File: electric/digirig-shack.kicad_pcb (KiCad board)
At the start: 2 copper layers, 80 x 50 mm, 63 parts, among them J1 USB_B_Micro, J2 USB_A, J3 PTT/CW, J4 Serial, J5 Audio, T1 600/600 Audio, T2 600/600 Audio, U1 TUSB2046, U2 CM108, U3 CP2102N-A01, U4 PC817, U5 PC817, Y1 6MHz, Y2 12MHz

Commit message: Rev 1.1 Mods Continued
Compressed mobile version to 23mm width
Added pulldown resistors on secondary USB ports in shack version
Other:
- board text added: "Rev 1.1"
- board text added: "by KW0X"
- board text added: "digirig shack"
- board text removed: "Rev 1.0"
- board text removed: "by KF0BAY"
- board text removed: "digirig"

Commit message: Revision 1.3 updates
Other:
- board text added: "by K0TX"
- board text removed: "by KW0X"

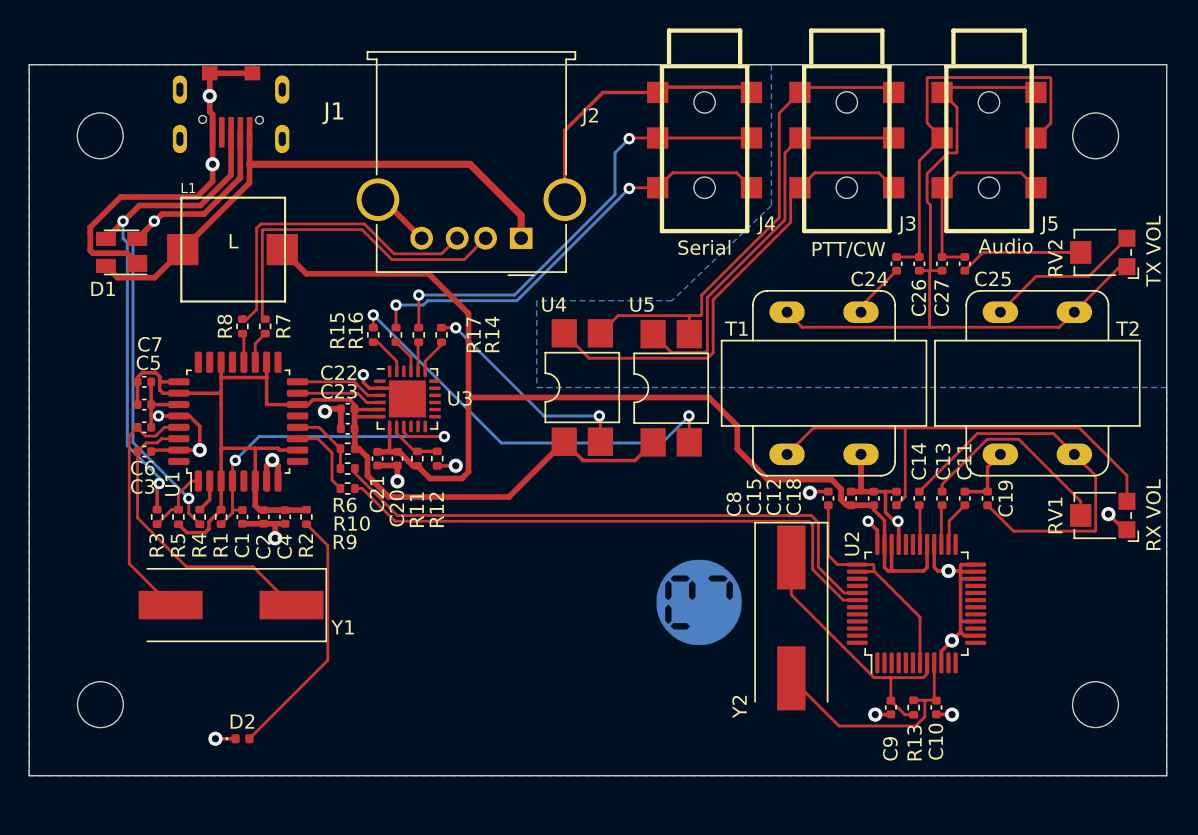
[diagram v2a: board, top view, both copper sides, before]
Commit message: Digirig Shack Rev 1.1
- 51mm wide board for sized aluminum case
- electric insulation on PC side instead of audio transformers
- Full size USB B connector on PC side
- RJ45 connector on rig side
- DIP socket for connector pinout configuration
- additional audio and serial pins as headers
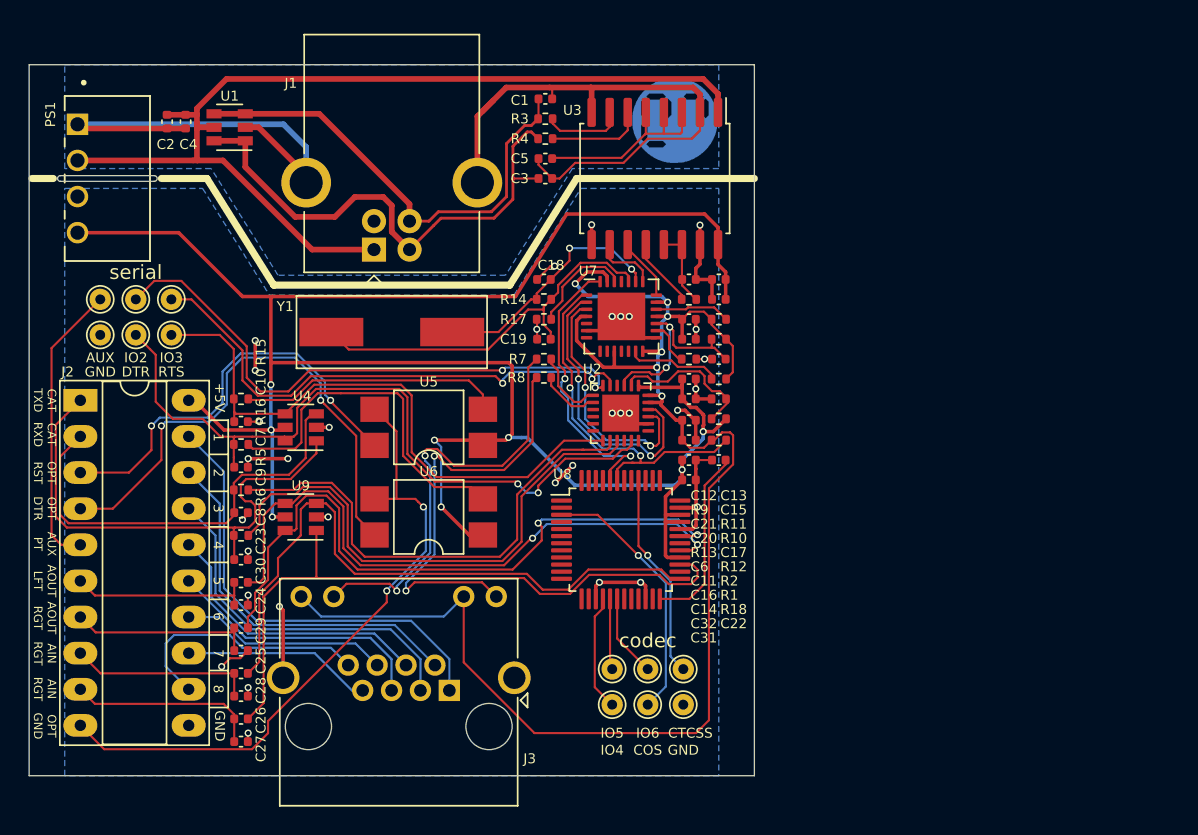
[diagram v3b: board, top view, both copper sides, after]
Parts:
- removed the C11 at (205.8, 69.5)
- removed the C14 at (202.6, 69.5)
- removed the C6 at (148.1, 64.5)
- removed D1: SP0503BAHT, Package_TO_SOT_SMD:SOT-143
- removed D2: PWR (RED), LED_SMD:LED_0402_1005Metric
- removed J4: Serial, footprints:jack_3.5_pj313d-smt
- removed J5: Audio, footprints:jack_3.5_pj313d-smt
- removed the R10 at (162.4, 67.4)
- removed RV1, RV2: 10K, Potentiometer_SMD:Potentiometer_Bourns_TC33X_Vertical
- removed Ref**: Val**, footprints:QR-code
- removed Ref**: Val**, footprints:digirig-logo-6mm
- removed T1, T2: 600/600 Audio, footprints:Audio_Transformer
- removed the U2 at (202.4, 76.9)
- removed Y2: 12MHz, Crystal:Crystal_SMD_HC49-SD
- added C1: 47pF, Capacitor_SMD:C_0402_1005Metric, F.Cu at (176.3, 41.4)
- added C2: 10uF, Capacitor_SMD:C_0402_1005Metric, F.Cu at (149.7, 43.0)
- added C22: 10uF, Capacitor_SMD:C_0402_1005Metric, F.Cu at (188.5, 66.8)
- added C23: 10uF, Capacitor_SMD:C_0402_1005Metric, F.Cu at (154.9, 75.4)
- added C28: 47pF, Capacitor_SMD:C_0402_1005Metric, F.Cu at (154.9, 83.4)
- added C29: 47pF, Capacitor_SMD:C_0402_1005Metric, F.Cu at (154.9, 80.2)
- added C30: 47pF, Capacitor_SMD:C_0402_1005Metric, F.Cu at (154.9, 77.0)
- added C31: 10uF, Capacitor_SMD:C_0402_1005Metric, F.Cu at (186.4, 68.2)
- added C32: 100nF, Capacitor_SMD:C_0402_1005Metric, F.Cu at (186.4, 66.8)
- added C4: 100nF, Capacitor_SMD:C_0402_1005Metric, F.Cu at (151.0, 43.0)
- added PS1: B0505S-1WR2, footprints:CONV_B0505S-1WR2, F.Cu at (145.5, 47.0)
- added R1: 22K, Resistor_SMD:R_0402_1005Metric, F.Cu at (188.5, 63.9)
- added R18: 1.5K, Resistor_SMD:R_0402_1005Metric, F.Cu at (188.5, 65.4)
- added TP1: IO3, TestPoint:TestPoint_THTPad_D1.5mm_Drill0.7mm, F.Cu at (150.0, 55.5)
- added TP10: IO6, TestPoint:TestPoint_THTPad_D1.5mm_Drill0.7mm, F.Cu at (183.5, 81.5)
- added TP11: GND, TestPoint:TestPoint_THTPad_D1.5mm_Drill0.7mm, F.Cu at (186.0, 84.0)
- added TP12: GND, TestPoint:TestPoint_THTPad_D1.5mm_Drill0.7mm, F.Cu at (145.0, 58.0)
- added TP2: IO2, TestPoint:TestPoint_THTPad_D1.5mm_Drill0.7mm, F.Cu at (147.5, 55.5)
- added TP3: RTS, TestPoint:TestPoint_THTPad_D1.5mm_Drill0.7mm, F.Cu at (150.0, 58.0)
- added TP4: DTR, TestPoint:TestPoint_THTPad_D1.5mm_Drill0.7mm, F.Cu at (147.5, 58.0)
- added TP5: AUX, TestPoint:TestPoint_THTPad_D1.5mm_Drill0.7mm, F.Cu at (145.0, 55.5)
- added TP6: COS, TestPoint:TestPoint_THTPad_D1.5mm_Drill0.7mm, F.Cu at (183.5, 84.0)
- added TP7: CTCSS, TestPoint:TestPoint_THTPad_D1.5mm_Drill0.7mm, F.Cu at (186.0, 81.5)
- added TP8: IO4, TestPoint:TestPoint_THTPad_D1.5mm_Drill0.7mm, F.Cu at (181.0, 84.0)
- added TP9: IO5, TestPoint:TestPoint_THTPad_D1.5mm_Drill0.7mm, F.Cu at (181.0, 81.5)
- added U3: ADUM3160, Package_SO:SOIC-16W_7.5x10.3mm_P1.27mm, F.Cu at (184.0, 47.0)
- added U4: ESDU5V0H4, Package_TO_SOT_SMD:SOT-23-6, F.Cu at (159.1, 64.5)
- added U7: USB2412-DZK-TR, Package_DFN_QFN:QFN-28-1EP_5x5mm_P0.5mm_EP3.35x3.35mm, F.Cu at (181.7, 56.7)
- added U8: CM118B, Package_QFP:LQFP-48_7x7mm_P0.5mm, F.Cu at (181.6, 72.4)
- added U9: ESDU5V0H4, Package_TO_SOT_SMD:SOT-23-6, F.Cu at (159.1, 70.8)
- C10, C3, C9: value 27pF -> 47pF
- C12: value 10uF -> 100nF
- C18, C19: value 100pF -> 27pF
- C26: value 100pF -> 10uF
- C27: value 100pF -> 47pF
- C7: value 100nF -> 47pF
- C8: value 10uF -> 47pF
- J1: value USB_B_Micro -> USB_B; footprint footprints:USB_MICRO_A01SB141B1-298 -> Connector_USB:USB_B_OST_USB-B1HSxx_Horizontal
- J2: value USB_A -> Socket_20DIP; footprint Connector_USB:USB_A_Molex_67643_Horizontal -> Package_DIP:DIP-20_W7.62mm_Socket_LongPads
- J3: value PTT/CW -> RJ45_LED_Shielded; footprint footprints:jack_3.5_pj313d-smt -> Connector_RJ:RJ45_Amphenol_RJHSE538X
- L1: value 2.2mH -> LOGO; footprint footprints:CD74R -> footprints:digirig-logo-6mm
- R11: value 22K -> 100K
- R12: value 47K -> 100K
- R13: value 1M -> 100K
- R14: value 470 -> 1M
- R16, R7, R8: value 33 -> 470
- R17: value 33 -> 12K
- R2: value 1K -> 47K
- R5, R6: value 1.5K -> 33
- R9: value 33 -> 10K
- U1: value TUSB2046 -> ESDU5V0H4; footprint Package_QFP:LQFP-32_7x7mm_P0.8mm -> Package_TO_SOT_SMD:SOT-23-6
- Y1: value 6MHz -> 24MHz
- moved C27 59.7 mm to (154.9, 86.6), turned to 180 degrees
- moved C25 58.5 mm to (154.9, 81.8), turned to 0 degrees
- moved C26 57.4 mm to (154.9, 85.0), turned to 0 degrees
- moved C10 52.9 mm to (154.9, 64.1), turned to 180 degrees
- moved C24 52.7 mm to (154.9, 78.6), turned to 0 degrees
- moved C9 47.7 mm to (154.9, 70.5), turned to 180 degrees
- moved J3 47.3 mm to (169.6, 83.0)
- moved C8 41.5 mm to (154.9, 73.8), turned to 180 degrees
- moved R3 39.1 mm to (176.3, 42.8), turned to 180 degrees
- moved R10 37.2 mm to (188.5, 58.3), turned to 0 degrees
- moved R4 36.0 mm to (176.3, 44.2), turned to 180 degrees
- moved C17 35.3 mm to (188.5, 59.7), turned to 180 degrees
- moved C3 34.1 mm to (176.3, 47.0)
- moved C19 33.1 mm to (176.2, 58.3), turned to 180 degrees
- moved C5 33.1 mm to (176.3, 45.6), turned to 180 degrees
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- renumbered C21 to C11, C22 to C14, C23 to C16, C1 to C17, C2 to C20, C4 to C21, C20 to C6, R1 to R10, U3 to U2, U4 to U5, U5 to U6
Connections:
- C10 pad 1: Net-(C10-Pad1) -> GND
- C10 pad 2: GND -> ~RTS
- C12 pad 1: +5V -> Net-(C12-Pad1)
- C13 pad 1: Net-(C13-Pad1) -> +5V
- C13 pad 2: Net-(C13-Pad2) -> GND
- C17 pad 1: /~RESET -> ~RESET
- C19 pad 1: GND -> Net-(C19-Pad1)
- C19 pad 2: Net-(C14-Pad1) -> GND
- C24 pad 1: /AIN -> AFOUT_RIGHT
- C25 pad 1: /AOUT -> AFIN_LEFT
- C26 pad 1: /AIN -> AFIN_RIGHT
- C26 pad 2: /IGND -> Net-(C26-Pad2)
- C27 pad 1: /IGND -> GND
- C27 pad 2: /AOUT -> AFIN_RIGHT
- C3 pad 1: Net-(C3-Pad1) -> /PC_N
- C3 pad 2: GND -> GND1
- C5 pad 1: +3V3 -> Net-(C5-Pad1)
- C5 pad 2: GND -> GND1
- C7 pad 1: +3V3 -> GND
- C7 pad 2: GND -> ~DTR
- C8 pad 1: Net-(C8-Pad1) -> GND
- C8 pad 2: GND -> TxD
- C9 pad 1: Net-(C9-Pad1) -> GND
- C9 pad 2: GND -> RxD
- J1 pad 1: /RAW5V -> +5P
- J1 pad 2: /DM_RAW -> /PC_N
- J1 pad 3: /DP_RAW -> /PC_P
- J1 pad 4: Net-(J1-Pad4) -> GND1
- J1 pad 5: GND -> GND1
- J2 pad 1: /RAW5V -> TxD
- J2 pad 2: Net-(J2-Pad2) -> RxD
- J2 pad 3: Net-(J2-Pad3) -> ~PTT
- J2 pad 4: GND -> ~KEY
- J2 pad 5: GND -> Net-(J2-Pad5)
- R10 pad 1: /~RESET -> ~RESET
- R11 pad 1: +5V -> +3V3
- R12 pad 1: Net-(R11-Pad2) -> +3V3
- R12 pad 2: GND -> Net-(R12-Pad2)
- R13 pad 1: Net-(C10-Pad1) -> Net-(R13-Pad1)
- R13 pad 2: Net-(C9-Pad1) -> GND
- R14 pad 1: Net-(R14-Pad1) -> Net-(C19-Pad1)
- R14 pad 2: Net-(R14-Pad2) -> Net-(C18-Pad1)
- R15 pad 2: Net-(R15-Pad2) -> ~RTS
- R16 pad 1: Net-(J4-PadT) -> Net-(R16-Pad1)
- R16 pad 2: Net-(R16-Pad2) -> ~DTR
- R17 pad 2: Net-(R17-Pad2) -> GND
- R2 pad 1: Net-(D2-Pad2) -> Net-(R1-Pad2)
- R2 pad 2: +3V3 -> GND
- R3 pad 2: /DP_RAW -> /PC_P
- R4 pad 2: /DM_RAW -> /PC_N
- R5 pad 1: Net-(R3-Pad1) -> RxD
- R5 pad 2: +3V3 -> Net-(R5-Pad2)
- R6 pad 1: Net-(R10-Pad2) -> TxD
- R6 pad 2: +3V3 -> Net-(R6-Pad2)
- R7 pad 1: Net-(J2-Pad2) -> ~RX_LED
- R8 pad 1: Net-(J2-Pad3) -> ~TX_LED
- R9 pad 1: Net-(R9-Pad1) -> Net-(C12-Pad1)
- U1 pad 1: Net-(R3-Pad1) -> /PC_N
- U1 pad 2: Net-(R4-Pad1) -> GND1
- U1 pad 3: +3V3 -> /PC_P
- U1 pad 4: /~RESET -> /PC_P
- U1 pad 5: Net-(U1-Pad5) -> +5P
- U1 pad 6: +3V3 -> /PC_N
- U2 pad 1: Net-(U3-Pad1) -> (no net)
- U2 pad 10: Net-(U3-Pad10) -> (no net)
- U2 pad 13: /~RX_LED -> Net-(R7-Pad2)
- U2 pad 14: /~TX_LED -> Net-(R8-Pad2)
- U2 pad 15: Net-(U3-Pad15) -> (no net)
- U2 pad 16: Net-(U3-Pad16) -> (no net)
- U2 pad 17: Net-(U3-Pad17) -> (no net)
- U2 pad 18: Net-(U3-Pad18) -> (no net)
- U2 pad 19: Net-(R14-Pad2) -> ~RTS
- U2 pad 20: Net-(R17-Pad2) -> Net-(R5-Pad2)
- U2 pad 21: Net-(R16-Pad2) -> Net-(R6-Pad2)
- U2 pad 22: Net-(U3-Pad22) -> (no net)
- U2 pad 23: Net-(R15-Pad2) -> ~DTR
- U2 pad 24: Net-(U3-Pad24) -> (no net)
- U2 pad 3: Net-(U1-Pad16) -> SRL_P
- U2 pad 4: Net-(U1-Pad15) -> SRL_N
- U2 pad 8: Net-(R11-Pad2) -> Net-(R1-Pad2)
- U2 pad 9: /~RESET -> ~RESET
- U5 pad 1: +3V3 -> +5V
- U5 pad 2: Net-(R14-Pad1) -> Net-(R15-Pad1)
- U5 pad 3: Net-(J3-PadS) -> GND2
- U5 pad 4: Net-(J3-PadT) -> ~PTT
- U6 pad 1: +3V3 -> +5V
- U6 pad 2: Net-(R15-Pad1) -> Net-(R16-Pad1)
- U6 pad 3: Net-(J3-PadS) -> GND2
- U6 pad 4: Net-(J3-PadR) -> ~KEY
- Y1 pad 1: Net-(C3-Pad1) -> Net-(C18-Pad1)
- Y1 pad 2: Net-(C6-Pad1) -> Net-(C19-Pad1)
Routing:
- net +5V: track 79.6 -> 154.3 mm, vias 0 -> 8
- net GND1: track 0.00 -> 74.4 mm
- net +5P: track 0.00 -> 69.6 mm
- net GND: track 122.1 -> 61.5 mm, vias 19 -> 33
- net /IGND: track 52.9 -> 0.00 mm
- net ~DTR: track 0.00 -> 52.1 mm, vias 0 -> 2
- net Net-(C26-Pad2): track 0.00 -> 46.9 mm
- net GND2: track 0.00 -> 45.5 mm, vias 0 -> 2
- net Net-(C23-Pad2): track 0.00 -> 43.9 mm, vias 0 -> 2
- net Net-(C24-Pad2): track 3.96 -> 47.1 mm, vias 0 -> 2
- net ~RTS: track 0.00 -> 42.9 mm
- net Net-(R10-Pad1): track 41.5 -> 0.00 mm
- net Net-(R9-Pad1): track 40.4 -> 0.00 mm
- net Net-(TP2-Pad1): track 0.00 -> 40.1 mm, vias 0 -> 2
- net /RAW5V: track 39.1 -> 0.00 mm
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- added copper zone on B.Cu, net GND1
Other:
- board size 80 x 50 mm -> 51 x 50 mm
- net class Default: clearance 0.2 -> 0.15; trace_width 0.2 -> 0.15; via_dia 0.8 -> 0.5; via_drill 0.4 -> 0.3
- net class Power: clearance 0.2 -> 0.15
- rule trace_clearance: 0.2 -> 0.15
- board text added: "+5V"
- board text added: "1"
- board text added: "2"
- board text added: "3"
- board text added: "4"
- board text added: "5"
- board text added: "6"
- board text added: "7"
- board text added: "8"
- board text added: "AIN RGT"
- board text added: "AOUT LFT"
- board text added: "AOUT RGT"
- board text added: "AUX PT"
- board text added: "CAT RXD"
- board text added: "CAT TXD"
- board text added: "GND"
- board text added: "OPT DTR"
- board text added: "OPT GND"
- board text added: "OPT RST"
- board text added: "PC isolation"
- board text added: "Rev 1.2"
- board text added: "codec"
- board text added: "serial"
- board text removed: "RX VOL"
- board text removed: "Rev 1.1"
- board text removed: "TX VOL"
- board text removed: "scan me"

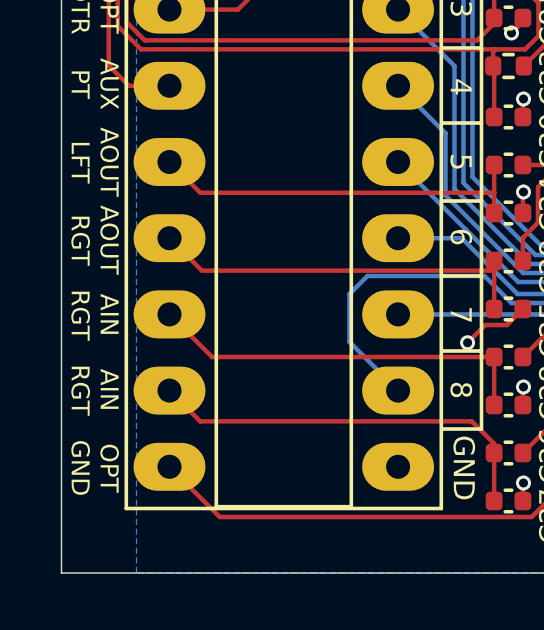
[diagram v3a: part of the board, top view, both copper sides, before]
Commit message: completed routing of plus version
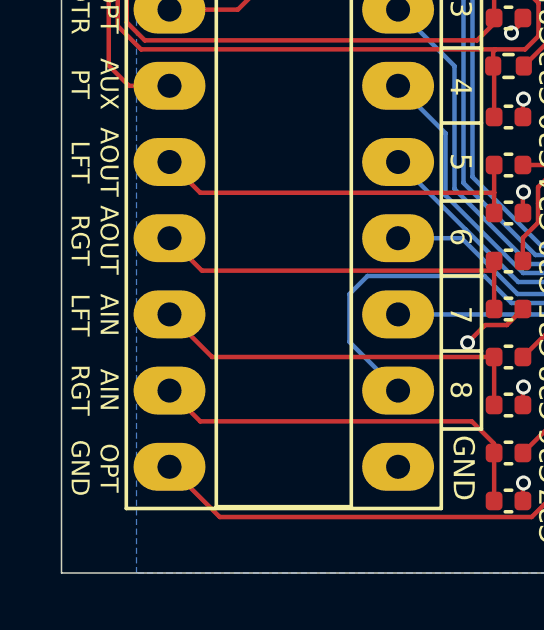
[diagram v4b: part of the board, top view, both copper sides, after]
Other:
- board text added: "AIN LFT"
